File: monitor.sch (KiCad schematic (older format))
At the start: 32 parts, among them J21 test, J22 test, J23 test, U16 XR2206, U17 TLP176A, U18 ANA4522

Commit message: 저항값설정
저항값 1차 설정
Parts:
- R159, R160: value 10k -> 1k
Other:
- note added: "Pair2 : R157, R160\nPair2 : R158, R159\nonly one pair needs to be soldered"
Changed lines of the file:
@@
 P 9650 4400
 F 0 "R160" V 9730 4400 50  0000 C CNN
-F 1 "10k" V 9650 4400 50  0000 C CNN
+F 1 "1k" V 9650 4400 50  0000 C CNN
 F 2 "Resistors_SMD:R_0805_HandSoldering" V 9580 4400 50  0001 C CNN
 F 3 "" H 9650 4400 50  0001 C CNN
@@
 P 9650 3250
 F 0 "R159" V 9730 3250 50  0000 C CNN
-F 1 "10k" V 9650 3250 50  0000 C CNN
+F 1 "1k" V 9650 3250 50  0000 C CNN
 F 2 "Resistors_SMD:R_0805_HandSoldering" V 9580 3250 50  0001 C CNN
 F 3 "" H 9650 3250 50  0001 C CNN
@@
 	-1   0    0    -1
 $EndComp
+Text Notes 8750 5400 0    60   ~ 0
+Pair2 : R157, R160\nPair2 : R158, R159\nonly one pair needs to be soldered
 $EndSCHEMATC

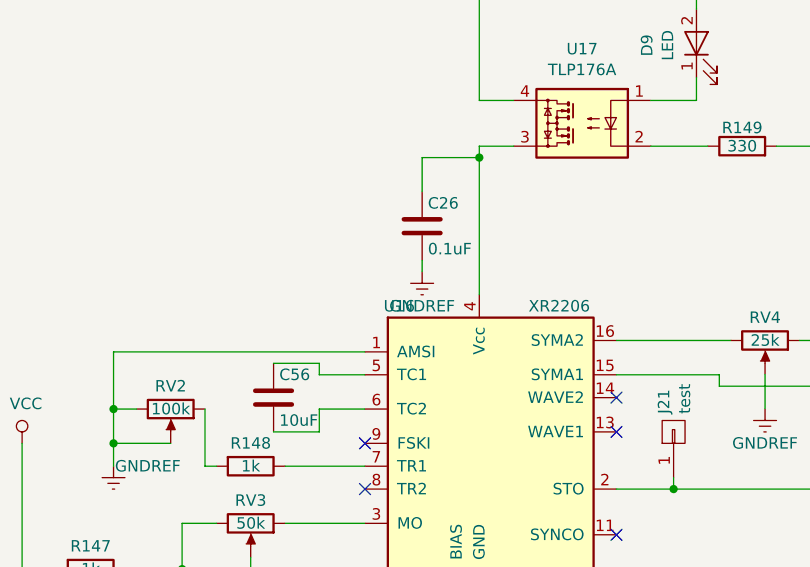
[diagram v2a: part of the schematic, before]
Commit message: 2차 PCB 1차 수정
1. ADR455 Vcc V12 수정
2. DCDC 입력전압 변경
3. Bypass 콘덴서 C66, C67 추가
4. SOIC 방향 표시
5. TLV431 PADS 변경
6. AQV258 Pin3 --> Pin2
7. 전해콘덴서 방향추가
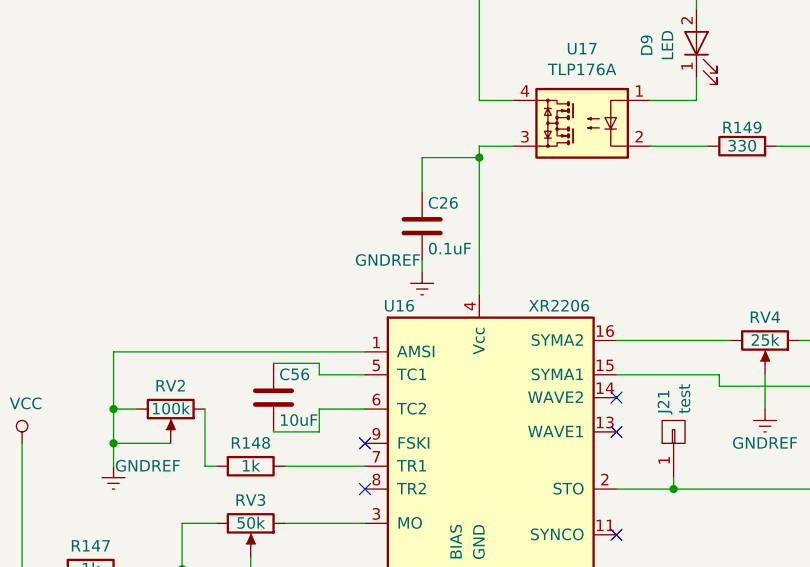
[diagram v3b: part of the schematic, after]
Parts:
- D10, D11: footprint TO_SOT_Packages_SMD:SOT-23 -> USER:SOT-23W_Handsoldering(LM431)
- U18: footprint Housings_SOIC:SOIC-8-1EP_3.9x4.9mm_Pitch1.27mm -> USER:SOIC-8_3.9x4.9mm_Pitch1.27mm
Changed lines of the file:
@@
 F 0 "U18" H 7750 5150 50  0000 L CNN
 F 1 "ANA4522" H 7700 4850 50  0000 L CNN
-F 2 "Housings_SOIC:SOIC-8-1EP_3.9x4.9mm_Pitch1.27mm" H 7750 5000 50  0001 C CNN
+F 2 "USER:SOIC-8_3.9x4.9mm_Pitch1.27mm" H 7750 5000 50  0001 C CNN
 F 3 "" H 7750 5000 50  0001 C CNN
 	2    7750 5000
@@
 F 0 "D10" V 6496 4831 50  0000 R CNN
 F 1 "TLV431DBZ" V 6405 4831 50  0000 R CNN
-F 2 "TO_SOT_Packages_SMD:SOT-23" H 6450 4750 50  0001 C CIN
+F 2 "USER:SOT-23W_Handsoldering(LM431)" H 6450 4750 50  0001 C CIN
 F 3 "" H 6450 4900 50  0001 C CNN
 	1    6450 4900
@@
 F 0 "U18" H 7750 2800 50  0000 L CNN
 F 1 "ANA4522" H 7750 2500 50  0000 L CNN
-F 2 "Housings_SOIC:SOIC-8-1EP_3.9x4.9mm_Pitch1.27mm" H 7750 2650 50  0001 C CNN
+F 2 "USER:SOIC-8_3.9x4.9mm_Pitch1.27mm" H 7750 2650 50  0001 C CNN
 F 3 "" H 7750 2650 50  0001 C CNN
 	1    7750 2650
@@
 F 0 "D11" V 6546 3531 50  0000 R CNN
 F 1 "TLV431DBZ" V 6455 3531 50  0000 R CNN
-F 2 "TO_SOT_Packages_SMD:SOT-23" H 6500 3450 50  0001 C CIN
+F 2 "USER:SOT-23W_Handsoldering(LM431)" H 6500 3450 50  0001 C CIN
 F 3 "" H 6500 3600 50  0001 C CNN
 	1    6500 3600
@@
 P 3300 2850
 F 0 "#PWR0158" H 3300 2600 50  0001 C CNN
-F 1 "GNDREF" H 3300 2700 50  0000 C CNN
+F 1 "GNDREF" H 3450 2900 50  0000 C CNN
 F 2 "" H 3300 2850 50  0001 C CNN
 F 3 "" H 3300 2850 50  0001 C CNN

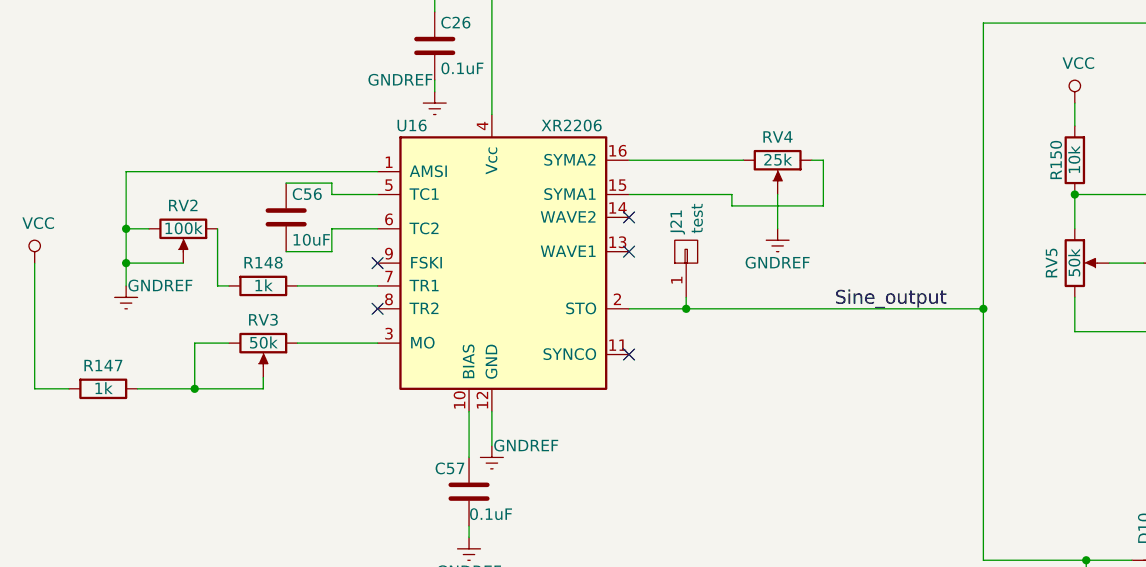
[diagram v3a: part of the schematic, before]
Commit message: Selector Numbering
Selector numbering
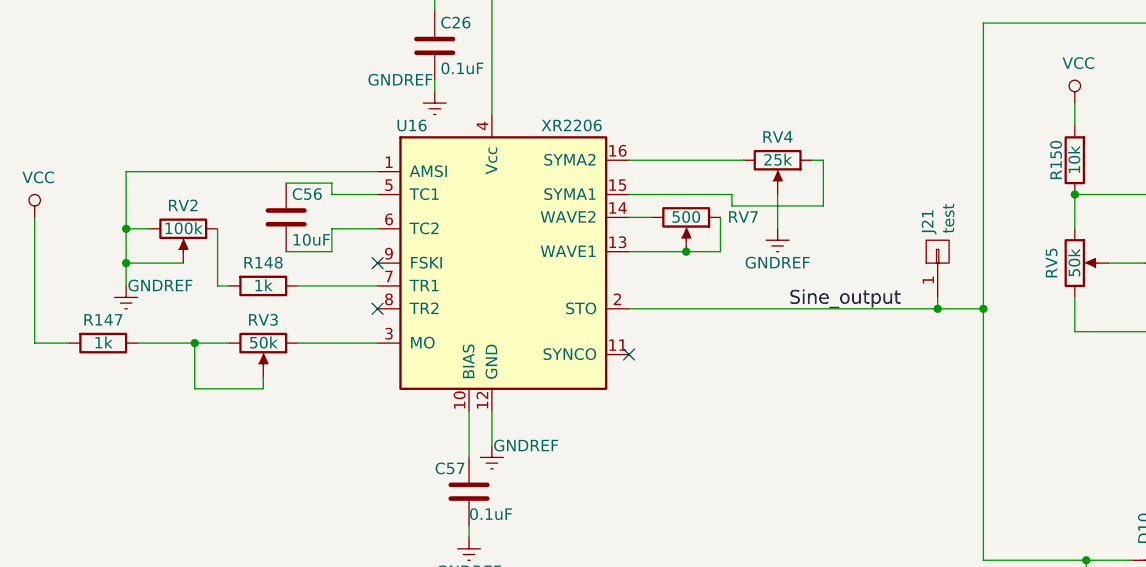
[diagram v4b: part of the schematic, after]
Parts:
- added RV7: 500, Potentiometers:Potentiometer_Trimmer_Bourns_3296W, symbol POT
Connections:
- net at U16.13 (WAVE1): now also RV7.1, RV7.2
- net at U16.14 (WAVE2): now also RV7.3
- no-connect marks 5 -> 3
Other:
- moved on the sheet: J21, R147
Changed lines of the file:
@@
 	2250 3950 2250 4150
 Wire Wire Line
-	2000 4150 2550 4150
-Wire Wire Line
 	2550 4150 2550 4100
 Wire Wire Line
@@
 Wire Wire Line
 	2350 3450 2350 3700
-Connection ~ 2250 4150
 Wire Wire Line
 	3550 2300 3550 2950
@@
 Wire Wire Line
 	4850 2300 5100 2300
-Connection ~ 4400 3800
+Connection ~ 5500 3800
 Wire Wire Line
 	4150 3800 5700 3800
@@
 L CONN_01X01 J21
 U 1 1 5B077AF7
-P 4400 3550
-F 0 "J21" H 4479 3592 50  0000 L CNN
-F 1 "test" H 4479 3501 50  0000 L CNN
-F 2 "Pin_Headers:Pin_Header_Straight_1x01_Pitch2.00mm" H 4400 3550 50  0001 C CNN
-F 3 "~" H 4400 3550 50  0001 C CNN
-	1    4400 3550
+P 5500 3550
+F 0 "J21" H 5579 3592 50  0000 L CNN
+F 1 "test" H 5579 3501 50  0000 L CNN
+F 2 "Pin_Headers:Pin_Header_Straight_1x01_Pitch2.00mm" H 5500 3550 50  0001 C CNN
+F 3 "~" H 5500 3550 50  0001 C CNN
+	1    5500 3550
 	0    -1   -1   0
 $EndComp
@@
 NoConn ~ 3050 3800
 NoConn ~ 3050 3600
-NoConn ~ 4150 3400
-NoConn ~ 4150 3550
-Wire Wire Line
-	1550 3600 1550 4150
+Wire Wire Line
+	1550 3400 1550 3950
 $Comp
 L VCC #PWR0118
 U 1 1 5B093B38
-P 1550 3600
-F 0 "#PWR0118" H 1550 3450 50  0001 C CNN
-F 1 "VCC" H 1567 3773 50  0000 C CNN
-F 2 "" H 1550 3600 50  0001 C CNN
-F 3 "" H 1550 3600 50  0001 C CNN
-	1    1550 3600
+P 1550 3400
+F 0 "#PWR0118" H 1550 3250 50  0001 C CNN
+F 1 "VCC" H 1567 3573 50  0000 C CNN
+F 2 "" H 1550 3400 50  0001 C CNN
+F 3 "" H 1550 3400 50  0001 C CNN
+	1    1550 3400
 	1    0    0    -1
 $EndComp
@@
 Connection ~ 6150 4900
 Wire Wire Line
-	4400 3800 4400 3750
+	5500 3800 5500 3750
 $Comp
 L R R147
 U 1 1 5B097651
-P 1850 4150
-F 0 "R147" V 1750 4150 50  0000 C CNN
-F 1 "1k" V 1850 4150 50  0000 C CNN
-F 2 "Resistors_SMD:R_0805_HandSoldering" V 1780 4150 50  0001 C CNN
-F 3 "" H 1850 4150 50  0001 C CNN
-	1    1850 4150
+P 1850 3950
+F 0 "R147" V 1750 3950 50  0000 C CNN
+F 1 "1k" V 1850 3950 50  0000 C CNN
+F 2 "Resistors_SMD:R_0805_HandSoldering" V 1780 3950 50  0001 C CNN
+F 3 "" H 1850 3950 50  0001 C CNN
+	1    1850 3950
 	0    1    1    0
 $EndComp
 Wire Wire Line
-	1550 4150 1700 4150
-Wire Wire Line
-	2250 3950 2400 3950
+	1550 3950 1700 3950
+Wire Wire Line
+	2000 3950 2400 3950
 Wire Wire Line
 	5700 2550 6750 2550
-Text Label 5050 3800 0    60   ~ 0
+Text Label 4850 3800 0    60   ~ 0
 Sine_output
 $Comp
@@
 Text Notes 8750 5400 0    60   ~ 0
 Pair2 : R157, R160\nPair2 : R158, R159\nonly one pair needs to be soldered
+$Comp
+L POT RV7
+U 1 1 5B207D04
+P 4400 3400
+F 0 "RV7" V 4400 3650 50  0000 C CNN
+F 1 "500" V 4400 3400 50  0000 C CNN
+F 2 "Potentiometers:Potentiometer_Trimmer_Bourns_3296W" H 4400 3400 50  0001 C CNN
+F 3 "" H 4400 3400 50  0001 C CNN
+	1    4400 3400
+	0    1    1    0
+$EndComp
+Wire Wire Line
+	4150 3400 4250 3400
+Wire Wire Line
+	4150 3550 4550 3550
+Wire Wire Line
+	4550 3550 4550 3400
+Connection ~ 4400 3550
+Connection ~ 2250 3950
+Wire Wire Line
+	2250 4150 2550 4150
 $EndSCHEMATC

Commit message: 4차 PCB
U23 Wire Breakage Relay 추가
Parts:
- U17: footprint Housings_SOIC:SO-4_4.4x4.3mm_Pitch2.54mm -> USER:SO-4_4.4x4.3mm_Pitch2.54mm_Hand_Soldering
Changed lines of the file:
@@
 F 0 "U17" H 4000 2525 50  0000 C CNN
 F 1 "TLP176A" H 4000 2434 50  0000 C CNN
-F 2 "Housings_SOIC:SO-4_4.4x4.3mm_Pitch2.54mm" H 3800 2000 50  0001 L CIN
+F 2 "USER:SO-4_4.4x4.3mm_Pitch2.54mm_Hand_Soldering" H 3800 2000 50  0001 L CIN
 F 3 "" H 3950 2200 50  0001 L CNN
 	1    4000 2200
